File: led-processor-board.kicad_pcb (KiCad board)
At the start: 2 copper layers, 100 x 89.5 mm, 127 parts, among them J1 USB-C, J2 SPARE, J3 SWD, J4 12V IN, J5 OUT1, J6 OUT2, J7 OUT3, J8 OUT4, J9 WL_GPIO, SW1 TS-1088R-02526, SW2 TS-1088R-02526, U1 RP2350B, U2 NCP1117ST33T3G, U3 W25Q128JVSIQ, U4 APS6404L-3SQR-SN, U5 RM2, U6 DS3231SN, U7 TPS54202H, X1 12MHz

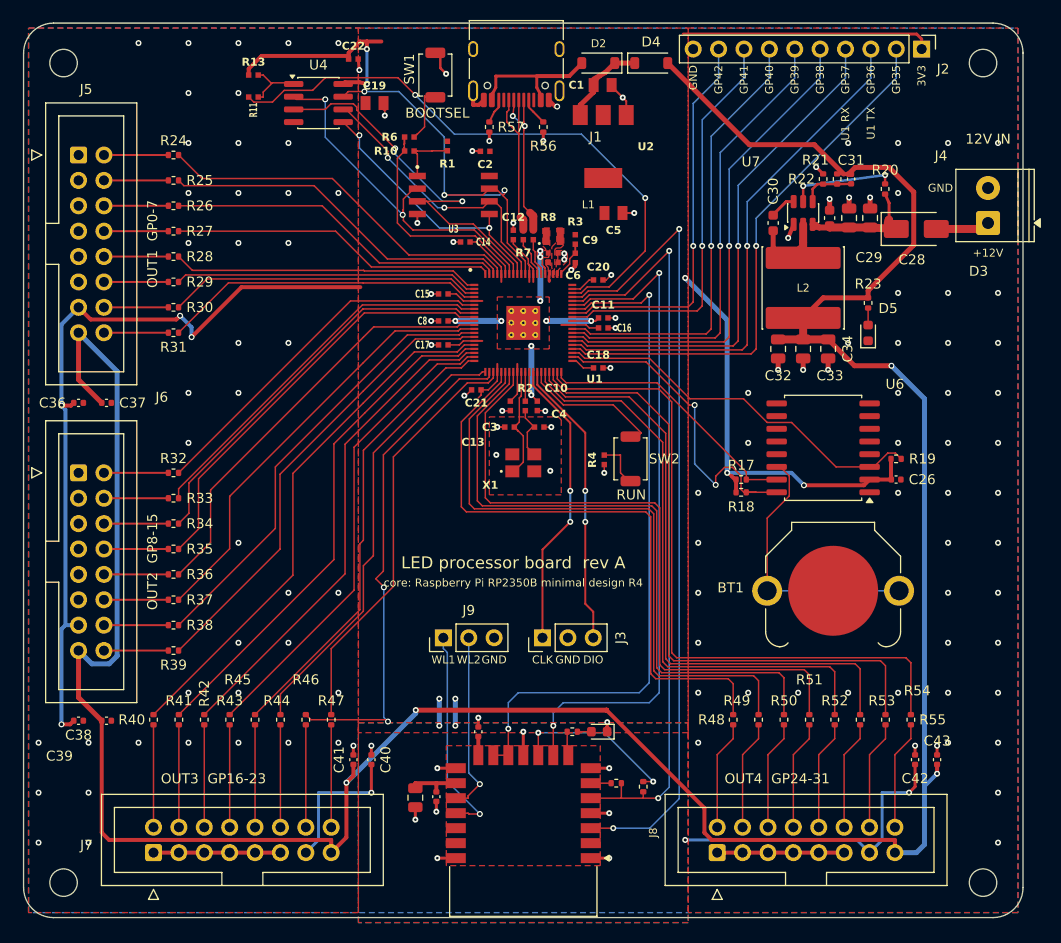
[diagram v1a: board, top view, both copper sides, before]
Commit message: v1.1 silkscreen: put every reference next to its own part
L1 (hand-soldered core inductor) gets a 1 mm label right above it and its
pin-1 dot moves to the middle of pad 1's side. The rest of the refs are
re-placed by tools/pcb/silk_near.py, which keeps each label nearest its own
part and clear of pads, silk and other labels; the dense spots (R7/R8,
buck feedback row, OUT3/OUT4 series resistors, J5/J6) are placed by hand in
its FIXED table. C6, C7 and C29 stay unlabelled (no spot that reads
clearly). Board text now says v1.1.

tools/pcb/silk_preview.py renders the silkscreen as fabbed; before/after
images in docs/silk-v1.1/. DRC: same 4 silk-edge warnings and 42 library
warnings as v1, no new items, 0 unconnected.

Co-Authored-By: Claude Opus 5.5 <noreply@anthropic.com>
Claude-Session: https://claude.ai/code/session_01NSi48cydvQ6UvBo4im78hn
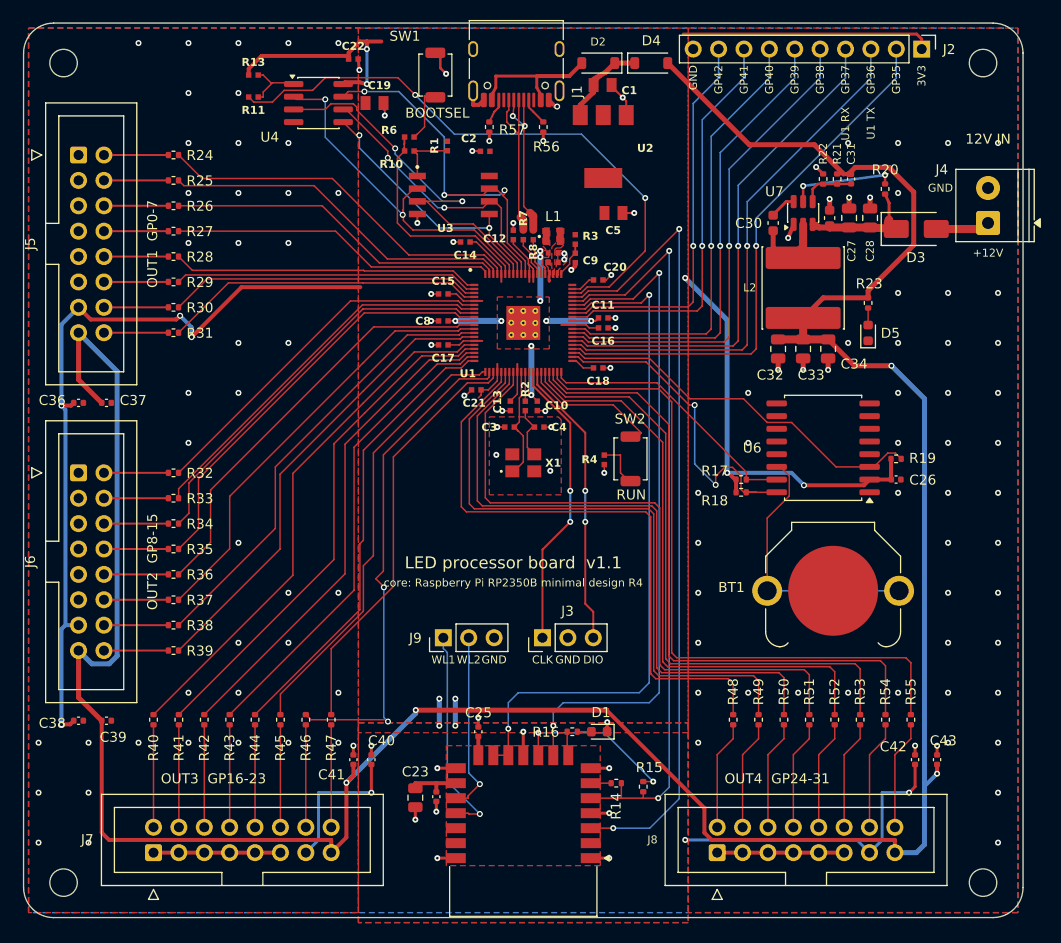
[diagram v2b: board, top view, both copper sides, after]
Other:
- board text added: "LED processor board v1.1"
- board text removed: "LED processor board rev A"
